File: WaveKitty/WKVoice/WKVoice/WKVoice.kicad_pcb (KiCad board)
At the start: 2 copper layers, 94.6 x 74.3 mm, 70 parts, among them J1 Conn, J2 Debug, J3 AudioJack3, J4 Conn_01x03, U1 ATmega328P-PU, U2 LM358, U3 LM358, Y1 Crystal

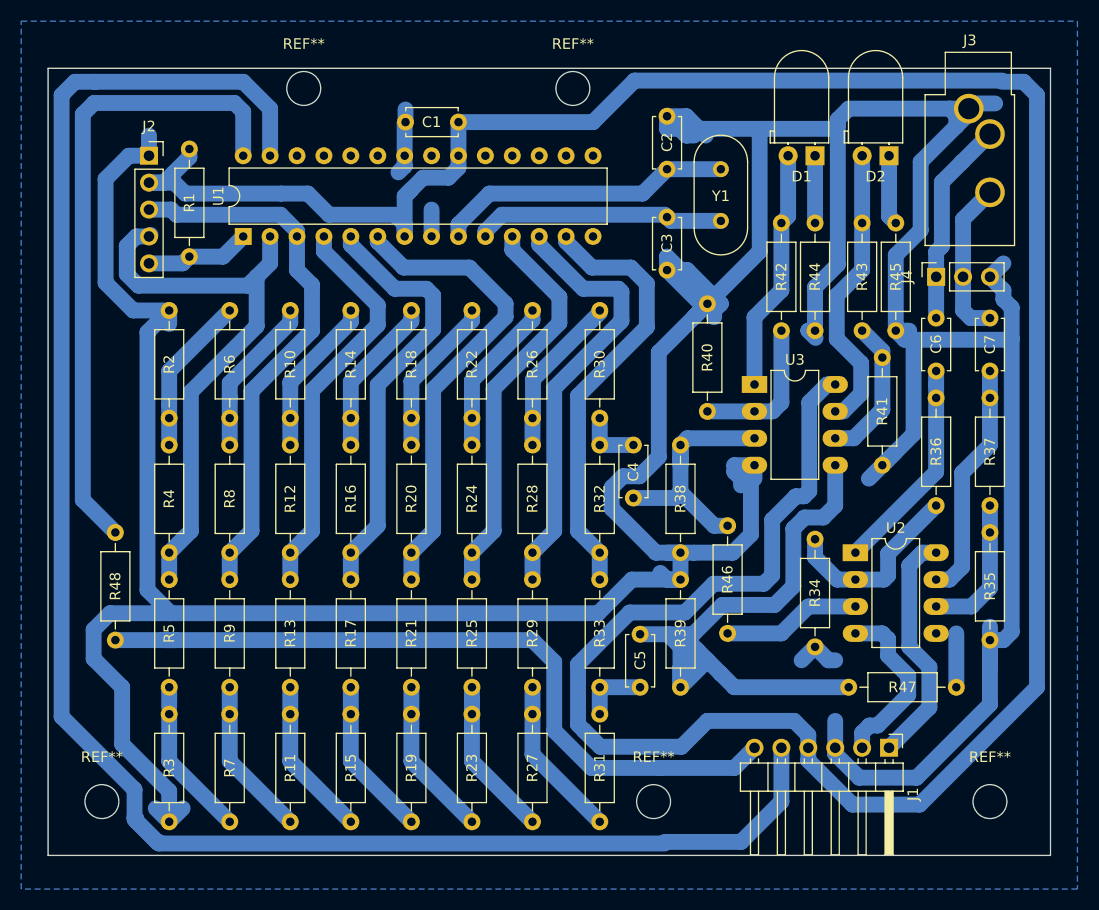
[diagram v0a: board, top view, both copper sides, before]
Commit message: Initial work on BitBug
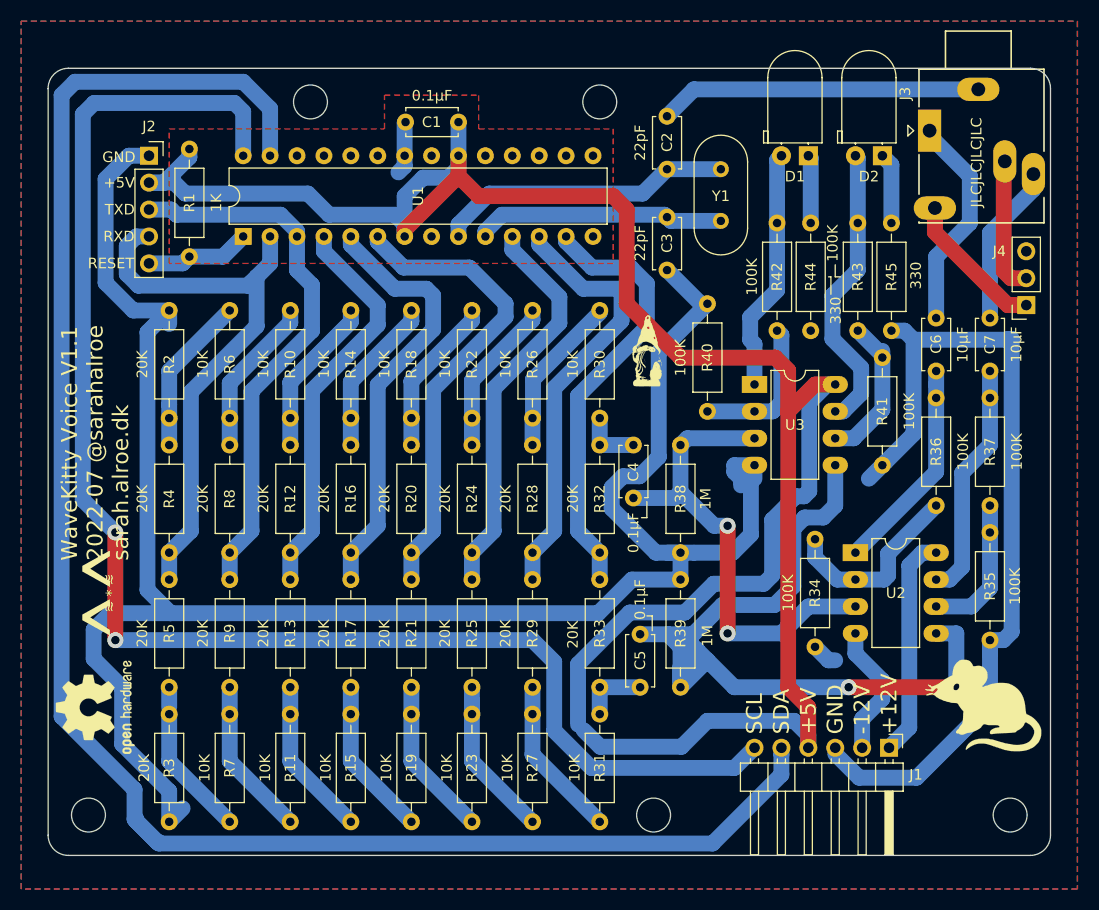
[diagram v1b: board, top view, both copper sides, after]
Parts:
- removed R46, R47, R48: 0, Resistor_THT:R_Axial_DIN0207_L6.3mm_D2.5mm_P10.16mm_Horizontal
- added G***: LOGO, logos:Gnome, F.Cu at (80.0, 53.3)
- added G***: LOGO, logos:Mouse, F.Cu at (111.8, 85.9)
- added REF**: OSHW-Logo2_9.8x8mm_SilkScreen, Symbol:OSHW-Logo2_9.8x8mm_SilkScreen, F.Cu at (27.9, 87.0)
- J3: value AudioJack3 -> AudioJack3_SwitchTR; footprint Connector_Audio:Jack_3.5mm_CUI_SJ1-3533NG_Horizontal_CircularHoles -> Connector_Audio:Jack_3.5mm_Ledino_KB3SPRS_Horizontal
- R10, R11, R14, R15, R18, R19, R22, R23, R26, R27, R30, R31, R6, R7: value 100K -> 10K
- R12, R13, R16, R17, R2, R20, R21, R24, R25, R28, R29, R3, R32, R33, R4, R5, R8, R9: value 200K -> 20K
- R34: value 10K -> 100K
- R35: value 18K -> 100K
- R36: value 68k -> 100K
- R37: value 68K -> 100K
- moved J4 8.92 mm to (115.8, 49.0), turned to 180 degrees
- moved J3 4.24 mm to (106.7, 32.6), turned to -90 degrees
- moved REF** 2.84 mm to (75.6, 29.8)
- moved REF** 2.29 mm to (114.3, 97.2)
- moved REF** 1.80 mm to (27.3, 97.2)
- moved REF** 1.42 mm to (48.3, 29.8)
- moved REF** 1.27 mm to (80.6, 97.2)
- moved D1 0.63 mm to (95.3, 34.9)
- moved D2 0.63 mm to (102.2, 34.9)
- moved R42 0.41 mm to (92.3, 41.3)
- moved R43 0.41 mm to (99.9, 41.3)
- moved R44 0.41 mm to (95.5, 51.4)
- moved R45 0.41 mm to (103.1, 51.4)
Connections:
- C6 pad 2: Net-(C6-Pad2) -> Net-(J3-PadT)
- C7 pad 2: Net-(C7-Pad2) -> Net-(J3-PadR)
- J1 pad 6: Net-(J1-Pad6) -> SCL
- J3 pad R: Net-(C7-Pad2) -> Net-(J3-PadR)
- J3 pad T: Net-(C6-Pad2) -> Net-(J3-PadT)
- J4 pad 1: Net-(C6-Pad2) -> Net-(J4-Pad1)
- J4 pad 2: Net-(C7-Pad2) -> Net-(J4-Pad2)
- U1 pad 14: Net-(U1-Pad14) -> unconnected-(U1-Pad14)
- U1 pad 15: Net-(U1-Pad15) -> unconnected-(U1-Pad15)
- U1 pad 16: Net-(U1-Pad16) -> unconnected-(U1-Pad16)
- U1 pad 17: Net-(U1-Pad17) -> unconnected-(U1-Pad17)
- U1 pad 18: Net-(U1-Pad18) -> unconnected-(U1-Pad18)
- U1 pad 19: Net-(U1-Pad19) -> unconnected-(U1-Pad19)
- U1 pad 21: Net-(U1-Pad21) -> unconnected-(U1-Pad21)
- U1 pad 23: Net-(U1-Pad23) -> unconnected-(U1-Pad23)
- U1 pad 24: Net-(U1-Pad24) -> unconnected-(U1-Pad24)
- U1 pad 25: Net-(U1-Pad25) -> unconnected-(U1-Pad25)
- U1 pad 26: Net-(U1-Pad26) -> unconnected-(U1-Pad26)
- U2 pad 3: Net-(R46-Pad2) -> DAC_OUT_L
- U2 pad 5: Net-(R47-Pad2) -> DAC_OUT_R
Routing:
- net GND: track 434.0 -> 314.5 mm
- net SCL: track 60.8 -> 140.9 mm, vias 0 -> 2
- net Net-(J1-Pad6): track 71.2 -> 0.00 mm
- net +5V: track 264.8 -> 215.8 mm
- net DAC_OUT_L: track 24.0 -> 45.4 mm, vias 0 -> 2
- net Net-(J3-PadT): track 0.00 -> 20.6 mm
- net Net-(C6-Pad2): track 19.5 -> 0.00 mm
- net DAC_OUT_R: track 61.5 -> 78.7 mm, vias 0 -> 2
- net Net-(J3-PadR): track 0.00 -> 15.3 mm
- net Net-(C7-Pad2): track 15.0 -> 0.00 mm
- net Net-(J4-Pad1): track 0.00 -> 13.8 mm
- net Net-(R46-Pad2): track 13.1 -> 0.00 mm
- net Net-(J4-Pad2): track 0.00 -> 12.8 mm
- net Net-(R47-Pad2): track 5.08 -> 0.00 mm
- net -12V: track 16.6 -> 12.6 mm
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- added copper zone on F.Cu, net +5V
- added copper zone on F.Cu, net GND
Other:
- outline, holes or cut-outs redrawn
- net class Default removed
- board text added: "*"
- board text added: "+12V"
- board text added: "+5V"
- board text added: "-12V"
- board text added: "GND"
- board text added: "JLCJLCJLCJLC"
- board text added: "RESET"
- board text added: "RXD"
- board text added: "SCL"
- board text added: "SDA"
- board text added: "TXD"
- board text added: "WaveKitty Voice V1.1 2022-07 @sarahalroe sarah.alroe.dk"
- board text added: "^^"
- board text added: "~"
